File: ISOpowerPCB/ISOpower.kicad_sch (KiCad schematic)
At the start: 10 parts, among them J1 XT60_connector_DC_60A_male, Q1 IRF5305_PBF

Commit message: adding logic for fault indication
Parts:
- F1: symbol 000_protection_immo:Fuse -> 000_Protection_Immo:Fuse
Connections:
- no-connect marks 0 -> 3
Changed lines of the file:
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@@
   (junction (at 73.66 34.29) (diameter 0) (color 0 0 0 0)
   )
+  (no_connect (at 247.65 86.36))
+  (no_connect (at 203.2 95.25))
+  (no_connect (at 203.2 92.71))
   (wire (pts (xy 168.91 93.98) (xy 168.91 97.79))
     (stroke (width 0) (type default) (color 0 0 0 0))
@@
     (stroke (width 0) (type default) (color 0 0 0 0))
   )
+  (wire (pts (xy 203.2 92.71) (xy 208.28 92.71))
+    (stroke (width 0) (type default) (color 0 0 0 0))
+  )
+  (wire (pts (xy 242.57 86.36) (xy 247.65 86.36))
+    (stroke (width 0) (type default) (color 0 0 0 0))
+  )
   (wire (pts (xy 158.75 105.41) (xy 158.75 60.96))
     (stroke (width 0) (type default) (color 0 0 0 0))
@@
   )
   (wire (pts (xy 240.03 124.46) (xy 240.03 129.54))
+    (stroke (width 0) (type default) (color 0 0 0 0))
+  )
+  (wire (pts (xy 203.2 95.25) (xy 208.28 95.25))
     (stroke (width 0) (type default) (color 0 0 0 0))
   )
@@
     (pin "1")
   )
-  (symbol (lib_id "000_protection_immo:Fuse") (at 45.72 34.29 90) (unit 1)
+  (symbol (lib_id "000_Protection_Immo:Fuse") (at 45.72 34.29 90) (unit 1)
     (in_bom yes) (on_board yes)
     (property "Reference" "F1" (id 0) (at 46.99 31.75 90)
@@
       (effects (font (size 1.27 1.27)) (justify left))
     )
-    (property "Footprint" "Fuse:Fuseholder_Cylinder-5x20mm_Stelvio-Kontek_PTF78_Horizontal_Open" (id 2) (at 45.72 36.068 90)
+    (property "Footprint" "Fuse:Fuseholder_Cylinder-5x20mm_Stelvio-Kontek_PTF78_Horizontal_Open" (id 2) (at 47.498 34.29 90)
       (effects (font (size 1.27 1.27)) hide)
     )
@@
       (reference "#PWR021") (unit 1) (value "GND") (footprint "")
     )
-    (path "/f713757b-9076-4778-b29c-f9f0971f0585/6d51a6b6-b0b3-456a-8b4a-183a83e2c722"
-      (reference "#PWR022") (unit 1) (value "GND1") (footprint "")
+    (path "/f713757b-9076-4778-b29c-f9f0971f0585/eaf33c28-b042-4795-8812-7a17e9144137"
+      (reference "#PWR022") (unit 1) (value "GND") (footprint "")
     )
     (path "/f713757b-9076-4778-b29c-f9f0971f0585/80a845a0-8fb7-4284-bef9-2b3e966f4d75"
@@
       (reference "#PWR092") (unit 1) (value "GND") (footprint "")
     )
+    (path "/4cdbbf68-1918-4084-bbdf-36d394700988/e7acea9a-1afc-4267-9991-eee6f99d5843"
+      (reference "#PWR?") (unit 1) (value "GND") (footprint "")
+    )
     (path "/f713757b-9076-4778-b29c-f9f0971f0585/bb1c97e7-f2b5-466c-8319-74aeab3f00d6"
       (reference "C1") (unit 1) (value "100n") (footprint "Capacitor_SMD:C_0805_2012Metric_Pad1.18x1.45mm_HandSolder")
@@
       (reference "D4") (unit 1) (value "PRTR5V0U2X") (footprint "Package_TO_SOT_SMD:SOT-143")
     )
+    (path "/4cdbbf68-1918-4084-bbdf-36d394700988/1ca5ed90-8a2f-4ac1-a059-4739d94f7ead"
+      (reference "D?") (unit 1) (value "GREEN") (footprint "")
+    )
+    (path "/4cdbbf68-1918-4084-bbdf-36d394700988/3c9283a0-55bc-4a02-a488-8eb66d9a2d3e"
+      (reference "D?") (unit 1) (value "RED") (footprint "")
+    )
     (path "/19ab4a26-652e-4198-91bc-8f059a723806"
       (reference "F1") (unit 1) (value "20A") (footprint "Fuse:Fuseholder_Cylinder-5x20mm_Stelvio-Kontek_PTF78_Horizontal_Open")
@@
       (reference "R30") (unit 1) (value "10k") (footprint "Resistor_SMD:R_0805_2012Metric_Pad1.20x1.40mm_HandSolder")
     )
+    (path "/4cdbbf68-1918-4084-bbdf-36d394700988/4ecf0738-9187-4c28-bb1e-946d67e207fb"
+      (reference "R?") (unit 1) (value "220r") (footprint "Resistor_SMD:R_0805_2012Metric_Pad1.20x1.40mm_HandSolder")
+    )
     (path "/f713757b-9076-4778-b29c-f9f0971f0585/1ea15eb9-713f-41fc-b81e-25ecc786fcca"
       (reference "SW1") (unit 1) (value "SW_Push") (footprint "")
@@
       (reference "U18") (unit 1) (value "TL431DBZ") (footprint "Package_TO_SOT_SMD:SOT-23")
     )
+    (path "/4cdbbf68-1918-4084-bbdf-36d394700988/63f43cda-9e3b-4393-868c-3b3f79f6a07a"
+      (reference "U?") (unit 1) (value "HEF4093B") (footprint "")
+    )
+    (path "/4cdbbf68-1918-4084-bbdf-36d394700988/86b6e28f-e51d-4ddf-8ccc-0759643a0cdf"
+      (reference "U?") (unit 2) (value "HEF4093B") (footprint "")
+    )
     (path "/f713757b-9076-4778-b29c-f9f0971f0585/3ec2a83f-7270-42d1-a1ce-a2b90a4b5cf1"

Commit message: fixed most electrical rules check violations
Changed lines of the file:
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@@
   (no_connect (at 203.2 95.25))
   (no_connect (at 203.2 92.71))
+  (wire (pts (xy 100.33 27.94) (xy 100.33 34.29))
+    (stroke (width 0) (type default) (color 0 0 0 0))
+  )
   (wire (pts (xy 168.91 93.98) (xy 168.91 97.79))
     (stroke (width 0) (type default) (color 0 0 0 0))
@@
     (stroke (width 0) (type default) (color 0 0 0 0))
   )
+  (wire (pts (xy 34.29 34.29) (xy 41.91 34.29))
+    (stroke (width 0) (type default) (color 0 0 0 0))
+  )
   (wire (pts (xy 203.2 92.71) (xy 208.28 92.71))
     (stroke (width 0) (type default) (color 0 0 0 0))
@@
   )
   (wire (pts (xy 176.53 127) (xy 176.53 116.84))
-    (stroke (width 0) (type default) (color 0 0 0 0))
-  )
-  (wire (pts (xy 34.29 34.29) (xy 41.91 34.29))
     (stroke (width 0) (type default) (color 0 0 0 0))
   )
@@
     (effects (font (size 3 3)) (justify left bottom))
   )
-  (text "Power Distribution & Dc/DC Conversion" (at 82.55 26.67 0)
+  (text "Power Distribution & Dc/DC Conversion" (at 82.55 19.05 0)
     (effects (font (size 3 3)) (justify left bottom))
   )
@@
       (effects (font (size 1.27 1.27)) (justify left))
     )
-    (property "Footprint" "Fuse:Fuseholder_Cylinder-5x20mm_Stelvio-Kontek_PTF78_Horizontal_Open" (id 2) (at 47.498 34.29 90)
+    (property "Footprint" "Fuse:Fuseholder_Cylinder-5x20mm_Stelvio-Kontek_PTF78_Horizontal_Open" (id 2) (at 45.72 36.068 90)
       (effects (font (size 1.27 1.27)) hide)
     )
@@
     (pin "1")
     (pin "2")
+  )
+  (symbol (lib_id "power:PWR_FLAG") (at 100.33 27.94 0) (unit 1)
+    (in_bom yes) (on_board yes) (fields_autoplaced)
+    (property "Reference" "#FLG01" (id 0) (at 100.33 26.035 0)
+      (effects (font (size 1.27 1.27)) hide)
+    )
+    (property "Value" "PWR_FLAG" (id 1) (at 100.33 22.86 0))
+    (property "Footprint" "" (id 2) (at 100.33 27.94 0)
+      (effects (font (size 1.27 1.27)) hide)
+    )
+    (property "Datasheet" "~" (id 3) (at 100.33 27.94 0)
+      (effects (font (size 1.27 1.27)) hide)
+    )
+    (pin "1")
   )
   (symbol (lib_id "power:GND") (at 38.1 67.31 0) (unit 1)
@@
       (effects (font (size 1.27 1.27)) (justify right))
     )
-    (property "Value" "XT60_connector_DC_60A_male" (id 1) (at 43.18 30.48 0)
+    (property "Value" "XT60_connector_DC_60A_male" (id 1) (at 41.91 30.48 0)
       (effects (font (size 1.27 1.27)) (justify right))
     )
@@
   )
   (symbol_instances
+    (path "/2543e485-176c-4822-b36b-ec39e8d80e95"
+      (reference "#FLG01") (unit 1) (value "PWR_FLAG") (footprint "")
+    )
+    (path "/f713757b-9076-4778-b29c-f9f0971f0585/7db0c078-80d1-4740-94ec-8b80a798cfe4"
+      (reference "#FLG02") (unit 1) (value "PWR_FLAG") (footprint "")
+    )
+    (path "/1f76f9be-4bce-499b-8dda-2796b250b412/4d17ea1d-89ed-4698-b52e-a81988c28d3c"
+      (reference "#FLG04") (unit 1) (value "PWR_FLAG") (footprint "")
+    )
+    (path "/1f76f9be-4bce-499b-8dda-2796b250b412/9b4eea19-5dc6-4c33-ab95-0e010a30282b"
+      (reference "#FLG05") (unit 1) (value "PWR_FLAG") (footprint "")
+    )
     (path "/d8f8abd1-528b-441f-9933-70b566445bad"
       (reference "#PWR01") (unit 1) (value "GND") (footprint "")
@@
       (reference "#PWR097") (unit 1) (value "GND") (footprint "")
     )
+    (path "/f713757b-9076-4778-b29c-f9f0971f0585/85b2bfc9-7e8e-4c8d-9249-1480bb828446"
+      (reference "#PWR0101") (unit 1) (value "GND") (footprint "")
+    )
     (path "/f713757b-9076-4778-b29c-f9f0971f0585/bb1c97e7-f2b5-466c-8319-74aeab3f00d6"
       (reference "C1") (unit 1) (value "100n") (footprint "Capacitor_SMD:C_0805_2012Metric_Pad1.18x1.45mm_HandSolder")
@@
     )
     (path "/4cdbbf68-1918-4084-bbdf-36d394700988/bcc18b17-96b9-48cd-932a-677e4d4ba0fe"
-      (reference "C30") (unit 1) (value "100n") (footprint "Capacitor_SMD:C_0805_2012Metric_Pad1.18x1.45mm_HandSolder")
+      (reference "C30") (unit 1) (value "100n") (footprint "Capacitor_SMD:CP_Elec_10x10")
     )
     (path "/e61c7578-28ab-439b-b249-5303c0f3bbca"
@@
     )
     (path "/f713757b-9076-4778-b29c-f9f0971f0585/a8f8f7fd-d3f8-4b42-968d-15db6e1251df"
-      (reference "L1") (unit 1) (value "L") (footprint "")
+      (reference "L1") (unit 1) (value "10uH") (footprint "")
     )
     (path "/1f76f9be-4bce-499b-8dda-2796b250b412/3246b713-6ea5-4f3d-8b80-f568a06c61c9"
@@
       (reference "U7") (unit 1) (value "ACS712xLCTR-30A") (footprint "Package_SO:SOIC-8_3.9x4.9mm_P1.27mm")
     )
-    (path "/1f76f9be-4bce-499b-8dda-2796b250b412/bd153913-7a36-4786-929e-d536aebcdfa3"
-      (reference "U8") (unit 5) (value "74HC02") (footprint "")
-    )
-    (path "/1f76f9be-4bce-499b-8dda-2796b250b412/4eedb16d-b390-4240-81c5-3391c298386a"
-      (reference "U9") (unit 5) (value "74HC02") (footprint "")
-    )
     (path "/1f76f9be-4bce-499b-8dda-2796b250b412/218e65a5-4797-4e02-b579-e8feacdd66d2"
       (reference "U10") (unit 1) (value "LM2596S-5") (footprint "Package_TO_SOT_SMD:TO-263-5_TabPin3")
     )
-    (path "/1f76f9be-4bce-499b-8dda-2796b250b412/f7aefa45-a645-4f75-baaf-bf6c09b8422c"
-      (reference "U11") (unit 5) (value "74HC02") (footprint "")
-    )
     (path "/f713757b-9076-4778-b29c-f9f0971f0585/435e8585-0aa6-45a8-a095-bd4d51e05765/beea1e48-0a65-4047-8cde-3d35fa41df31"

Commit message: Footprint Associations 50% complete
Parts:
- J1: footprint (none) -> Connector_AMASS:AMASS_XT60-M_1x02_P7.20mm_Vertical

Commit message: added documentation for component selection
Completed footprint association & added documentation re Netclasses. Need to update netclasses in schematic settings before moving to PCB layout.
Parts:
- added J21: 24vTerminal, TerminalBlock:TerminalBlock_Altech_AK300-2_P5.00mm, symbol Connector:Screw_Terminal_01x02
- added J22: 12vTerminal, TerminalBlock:TerminalBlock_Altech_AK300-2_P5.00mm, symbol Connector:Screw_Terminal_01x02
- added J23: 5vTerminal, TerminalBlock:TerminalBlock_Altech_AK300-2_P5.00mm, symbol Connector:Screw_Terminal_01x02
- Q1: footprint Package_TO_SOT_THT:TO-220-3_Vertical -> Package_TO_SOT_SMD:TO-263-2
- TP1, TP2, TP3, TP4, TP5: footprint (none) -> TestPoint:TestPoint_Pad_D1.5mm
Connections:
- net +12V_BUS: now also J22.2 (Pin_2)
- net +5V_BUS: now also J23.2 (Pin_2)
- net 24V_BUS: now also J21.2 (Pin_2)
- net GND: now also J21.1 (Pin_1), J22.1 (Pin_1), J23.1 (Pin_1)
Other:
- moved on the sheet: TP1

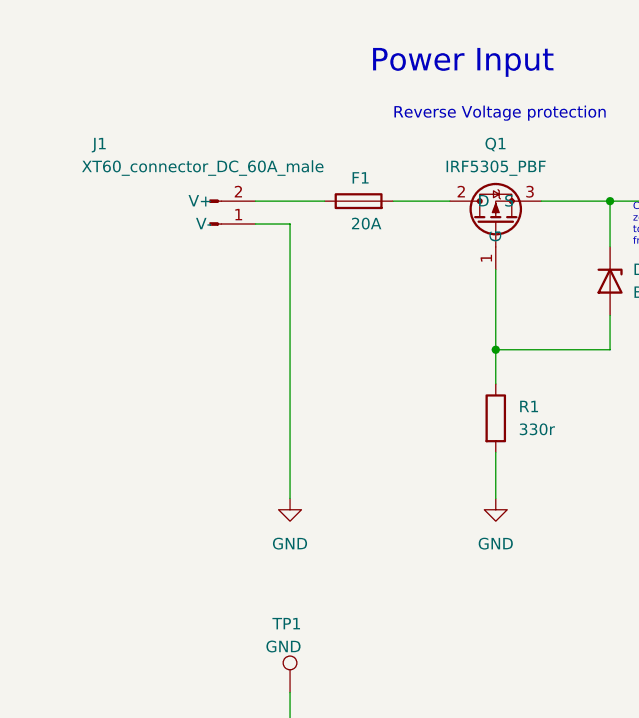
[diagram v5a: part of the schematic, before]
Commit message: added netclasses
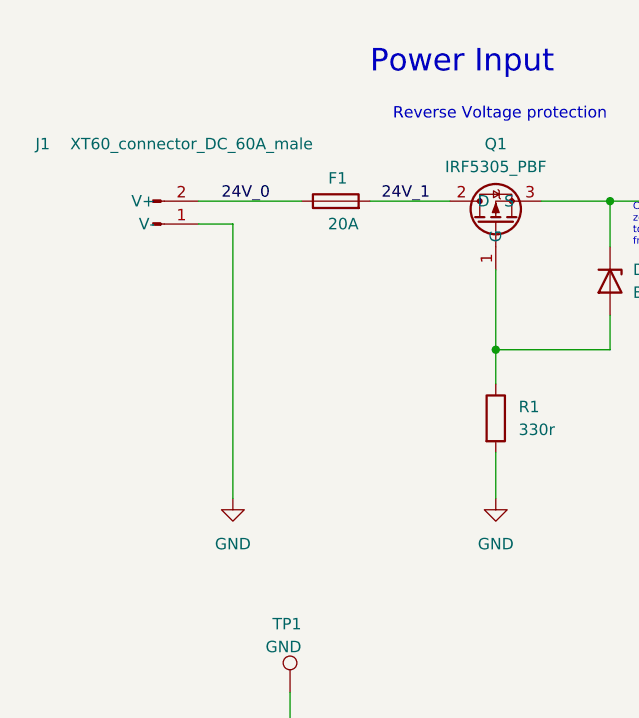
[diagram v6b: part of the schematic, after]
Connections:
- net 24V_0: now reaches F1.1, J1.2 (V+)
- net 24V_1: now reaches F1.2, Q1.2 (D)
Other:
- moved on the sheet: F1, J1
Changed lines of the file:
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@@
     (stroke (width 0) (type default) (color 0 0 0 0))
   )
-  (wire (pts (xy 49.53 34.29) (xy 55.88 34.29))
+  (wire (pts (xy 46.99 34.29) (xy 55.88 34.29))
     (stroke (width 0) (type default) (color 0 0 0 0))
   )
@@
     (stroke (width 0) (type default) (color 0 0 0 0))
   )
-  (wire (pts (xy 34.29 36.83) (xy 38.1 36.83))
+  (wire (pts (xy 27.94 36.83) (xy 31.75 36.83))
     (stroke (width 0) (type default) (color 0 0 0 0))
   )
@@
     (stroke (width 0) (type default) (color 0 0 0 0))
   )
-  (wire (pts (xy 34.29 34.29) (xy 41.91 34.29))
-    (stroke (width 0) (type default) (color 0 0 0 0))
-  )
   (wire (pts (xy 203.2 92.71) (xy 208.28 92.71))
     (stroke (width 0) (type default) (color 0 0 0 0))
@@
     (stroke (width 0) (type default) (color 0 0 0 0))
   )
+  (wire (pts (xy 27.94 34.29) (xy 39.37 34.29))
+    (stroke (width 0) (type default) (color 0 0 0 0))
+  )
   (wire (pts (xy 266.7 36.83) (xy 243.84 36.83))
     (stroke (width 0) (type default) (color 0 0 0 0))
@@
     (stroke (width 0) (type default) (color 0 0 0 0))
   )
-  (wire (pts (xy 38.1 36.83) (xy 38.1 67.31))
+  (wire (pts (xy 31.75 36.83) (xy 31.75 67.31))
     (stroke (width 0) (type default) (color 0 0 0 0))
   )
@@
   )
   (label "+5V_BUS" (at 180.4597 38.1 0)
+    (effects (font (size 1.27 1.27)) (justify left bottom))
+  )
+  (label "24V_1" (at 48.26 34.29 0)
+    (effects (font (size 1.27 1.27)) (justify left bottom))
+  )
+  (label "24V_0" (at 30.48 34.29 0)
     (effects (font (size 1.27 1.27)) (justify left bottom))
   )
@@
     (pin "2")
   )
-  (symbol (lib_id "000_Protection_Immo:Fuse") (at 45.72 34.29 90) (unit 1)
+  (symbol (lib_id "000_Protection_Immo:Fuse") (at 43.18 34.29 90) (unit 1)
     (in_bom yes) (on_board yes)
-    (property "Reference" "F1" (id 0) (at 46.99 31.75 90)
-      (effects (font (size 1.27 1.27)) (justify left))
-    )
-    (property "Value" "20A" (id 1) (at 48.26 36.83 90)
-      (effects (font (size 1.27 1.27)) (justify left))
-    )
-    (property "Footprint" "Fuse:Fuseholder_Cylinder-5x20mm_Stelvio-Kontek_PTF78_Horizontal_Open" (id 2) (at 45.72 36.068 90)
-      (effects (font (size 1.27 1.27)) hide)
-    )
-    (property "Datasheet" "~" (id 3) (at 45.72 34.29 0)
+    (property "Reference" "F1" (id 0) (at 44.45 31.75 90)
+      (effects (font (size 1.27 1.27)) (justify left))
+    )
+    (property "Value" "20A" (id 1) (at 45.72 36.83 90)
+      (effects (font (size 1.27 1.27)) (justify left))
+    )
+    (property "Footprint" "Fuse:Fuseholder_Cylinder-5x20mm_Stelvio-Kontek_PTF78_Horizontal_Open" (id 2) (at 43.18 36.068 90)
+      (effects (font (size 1.27 1.27)) hide)
+    )
+    (property "Datasheet" "~" (id 3) (at 43.18 34.29 0)
       (effects (font (size 1.27 1.27)) hide)
     )
@@
     (pin "1")
   )
-  (symbol (lib_id "power:GND") (at 38.1 67.31 0) (unit 1)
+  (symbol (lib_id "power:GND") (at 31.75 67.31 0) (unit 1)
     (in_bom yes) (on_board yes) (fields_autoplaced)
-    (property "Reference" "#PWR02" (id 0) (at 38.1 73.66 0)
-      (effects (font (size 1.27 1.27)) hide)
-    )
-    (property "Value" "GND" (id 1) (at 38.1 72.39 0))
-    (property "Footprint" "" (id 2) (at 38.1 67.31 0)
-      (effects (font (size 1.27 1.27)) hide)
-    )
-    (property "Datasheet" "" (id 3) (at 38.1 67.31 0)
+    (property "Reference" "#PWR02" (id 0) (at 31.75 73.66 0)
+      (effects (font (size 1.27 1.27)) hide)
+    )
+    (property "Value" "GND" (id 1) (at 31.75 72.39 0))
+    (property "Footprint" "" (id 2) (at 31.75 67.31 0)
+      (effects (font (size 1.27 1.27)) hide)
+    )
+    (property "Datasheet" "" (id 3) (at 31.75 67.31 0)
       (effects (font (size 1.27 1.27)) hide)
     )
@@
     (pin "1")
   )
-  (symbol (lib_id "000_Connectors_Immo:XT60_connector_DC_60A_male") (at 29.21 36.83 0) (mirror x) (unit 1)
+  (symbol (lib_id "000_Connectors_Immo:XT60_connector_DC_60A_male") (at 22.86 36.83 0) (mirror x) (unit 1)
     (in_bom yes) (on_board yes)
-    (property "Reference" "J1" (id 0) (at 17.78 27.94 0)
-      (effects (font (size 1.27 1.27)) (justify right))
-    )
-    (property "Value" "XT60_connector_DC_60A_male" (id 1) (at 41.91 30.48 0)
-      (effects (font (size 1.27 1.27)) (justify right))
-    )
-    (property "Footprint" "Connector_AMASS:AMASS_XT60-M_1x02_P7.20mm_Vertical" (id 2) (at 29.21 36.83 0)
-      (effects (font (size 1.27 1.27)) hide)
-    )
-    (property "Datasheet" "~" (id 3) (at 26.67 36.83 90)
+    (property "Reference" "J1" (id 0) (at 11.43 27.94 0)
+      (effects (font (size 1.27 1.27)) (justify right))
+    )
+    (property "Value" "XT60_connector_DC_60A_male" (id 1) (at 40.64 27.94 0)
+      (effects (font (size 1.27 1.27)) (justify right))
+    )
+    (property "Footprint" "Connector_AMASS:AMASS_XT60-M_1x02_P7.20mm_Vertical" (id 2) (at 22.86 36.83 0)
+      (effects (font (size 1.27 1.27)) hide)
+    )
+    (property "Datasheet" "~" (id 3) (at 20.32 36.83 90)
       (effects (font (size 1.27 1.27)) hide)
     )
@@
       (reference "#PWR042") (unit 1) (value "GND") (footprint "")
     )
-    (path "/1f76f9be-4bce-499b-8dda-2796b250b412/1a440712-5ded-4a84-8784-8a1af256858e"
+    (path "/1f76f9be-4bce-499b-8dda-2796b250b412/9e833acf-5225-492a-a451-09bb3d974b89"
       (reference "#PWR043") (unit 1) (value "+5V") (footprint "")
     )
-    (path "/1f76f9be-4bce-499b-8dda-2796b250b412/59419f56-90fa-47e5-984d-786ead8898c7"
+    (path "/1f76f9be-4bce-499b-8dda-2796b250b412/d8a40e66-9193-4ea0-bb90-6adefac55e31"
       (reference "#PWR044") (unit 1) (value "+12V") (footprint "")
     )
@@
     )
     (path "/f713757b-9076-4778-b29c-f9f0971f0585/148a063e-8854-4327-bddb-d4d3b5a6480c"
-      (reference "J6") (unit 1) (value "Conn_01x03_Male") (footprint "Connector_PinHeader_1.27mm:PinHeader_1x03_P1.27mm_Vertical")
+      (reference "J6") (unit 1) (value "prog_power_select") (footprint "Connector_PinHeader_1.27mm:PinHeader_1x03_P1.27mm_Vertical")
     )
     (path "/f713757b-9076-4778-b29c-f9f0971f0585/a29f83ae-9f84-45a9-8adc-6f0ffe47675b"
@@
     )
     (path "/f713757b-9076-4778-b29c-f9f0971f0585/9d614864-4d13-40f9-9129-6109f32998fd"
-      (reference "JP1") (unit 1) (value "Jumper_3_Bridged12") (footprint "Jumper:SolderJumper-3_P1.3mm_Bridged12_RoundedPad1.0x1.5mm_NumberLabels")
+      (reference "JP1") (unit 1) (value "prog_power_select") (footprint "Jumper:SolderJumper-3_P1.3mm_Bridged12_RoundedPad1.0x1.5mm_NumberLabels")
     )
     (path "/1f76f9be-4bce-499b-8dda-2796b250b412/dfb36977-98ef-40b5-824c-697cbf9bf5e9"
@@
       (reference "M1") (unit 1) (value "Fan_IEC60617") (footprint "ISOpower:Fan12V_40by10.5mm")
     )
+    (path "/1f76f9be-4bce-499b-8dda-2796b250b412/f31f2540-7987-42bf-9286-046529b027cd"
+      (reference "N1") (unit 1) (value "Net_Tie") (footprint "NetTie:NetTie-2_SMD_Pad0.5mm")
+    )
+    (path "/1f76f9be-4bce-499b-8dda-2796b250b412/1ba01dbc-6227-422d-8404-4b9d16e4915e"
+      (reference "N2") (unit 1) (value "Net_Tie") (footprint "NetTie:NetTie-2_SMD_Pad0.5mm")
+    )
     (path "/bd4eb304-3e85-4f2d-8568-e8105e1edb8e"

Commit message: PCB Layouts
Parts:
- added J24: dio_spare, Connector_PinHeader_1.27mm:PinHeader_1x01_P1.27mm_Vertical, symbol 000_Pin_Headers_Immo:Conn_01x01_Male
- added J25: adc_spare, Connector_PinHeader_1.27mm:PinHeader_1x02_P1.27mm_Vertical, symbol 000_Pin_Headers_Immo:Conn_01x02_Male
- added J26: USB_5v, Connector_PinHeader_1.27mm:PinHeader_1x01_P1.27mm_Vertical, symbol 000_Pin_Headers_Immo:Conn_01x01_Male
- added J27: pwr_ctls, Connector_PinSocket_1.27mm:PinSocket_1x05_P1.27mm_Vertical, symbol 000_Pin_Headers_Immo:Conn_01x05_Female
- added J28: MCU_DIO_A, Connector_PinHeader_1.27mm:PinHeader_1x05_P1.27mm_Vertical, symbol 000_Pin_Headers_Immo:Conn_01x05_Male
- added J29: sensor_op, Connector_PinSocket_1.27mm:PinSocket_1x04_P1.27mm_Vertical, symbol 000_Pin_Headers_Immo:Conn_01x04_Female
- added J30: MCU_ADC, Connector_PinHeader_1.27mm:PinHeader_1x04_P1.27mm_Vertical, symbol 000_Pin_Headers_Immo:Conn_01x04_Male
- added J31: main_pwr, Connector_PinSocket_1.27mm:PinSocket_1x05_P1.27mm_Vertical, symbol 000_Pin_Headers_Immo:Conn_01x05_Female
- added J32: MCU_PWR, Connector_PinHeader_1.27mm:PinHeader_1x05_P1.27mm_Vertical, symbol 000_Pin_Headers_Immo:Conn_01x05_Male
- added J33: MCU_DIO_B, Connector_PinHeader_1.27mm:PinHeader_1x05_P1.27mm_Vertical, symbol 000_Pin_Headers_Immo:Conn_01x05_Male
- added J34: O/P_ctls, Connector_PinSocket_1.27mm:PinSocket_1x05_P1.27mm_Vertical, symbol 000_Pin_Headers_Immo:Conn_01x05_Female
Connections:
- net 12V_BUS_MONITOR: now also J27.5 (Pin_5)
- net 5V_BUS_MONITOR: now also J27.4 (Pin_4)
- net BUS_A_DISABLE: now also J27.1 (Pin_1)
- net BUS_B_DISABLE: now also J27.2 (Pin_2)
- net BUS_I_SENSE_A: now also J29.1 (Pin_1)
- net BUS_I_SENSE_B: now also J29.2 (Pin_2)
- net GND: now also J31.1 (Pin_1)
- net MCU/ADC4: now also J30.4 (Pin_4)
- net MCU/ADC5: now also J30.3 (Pin_3)
- net MCU/CH_C: now also J28.3 (Pin_3)
- net MCU/CH_F: now also J33.1 (Pin_1)
- net MCU/CH_G: now also J33.2 (Pin_2)
- net MCU/CH_H: now also J33.3 (Pin_3)
- net MCU/CH_I: now also J33.4 (Pin_4)
- net MCU/CH_J: now also J33.5 (Pin_5)
- net MCU_5V: now also J31.3 (Pin_3)
- net +12V_BUS renamed 12V_BUS
- net +3V3_BUS renamed 3V3_BUS
- net 3V3_BUS: now also J31.2 (Pin_2)
- net +5V_BUS renamed 5V_BUS
- new net: J26.1 (Pin_1), J31.4 (Pin_4)
- new net: J25.1 (Pin_1), J29.3 (Pin_3)
- new net: J25.2 (Pin_2), J29.4 (Pin_4)
- new net: J24.1 (Pin_1), J27.3 (Pin_3)
- new net MCU/+5V_IN: J32.3 (Pin_3)
- new net MCU/3V3_OUT: J32.2 (Pin_2)
- new net MCU/ADC6: J30.2 (Pin_2)
- new net MCU/ADC7: J30.1 (Pin_1)
- new net MCU/CH_A: J28.1 (Pin_1)
- new net MCU/CH_B: J28.2 (Pin_2)
- new net MCU/GND: J32.1 (Pin_1)
- new net MCU/IN_D: J28.4 (Pin_4)
- new net MCU/IN_E: J28.5 (Pin_5)
- new net MCU/USB_POUT: J32.4 (Pin_4)
- new net Power Outputs/CH_F_CTRL: J34.1 (Pin_1)
- new net Power Outputs/CH_G_CTRL: J34.2 (Pin_2)
- new net Power Outputs/CH_H_CTRL: J34.3 (Pin_3)
- new net Power Outputs/CH_I_CTRL: J34.4 (Pin_4)
- new net Power Outputs/CH_J_CTRL: J34.5 (Pin_5)
- no-connect marks 3 -> 2
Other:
- sheet MCU ports: added USB_POUT; removed none
- note added: "Extra pin for future use, additionally, may make this module easier to plug in the correct way."
- moved on the sheet: TP1, TP3
